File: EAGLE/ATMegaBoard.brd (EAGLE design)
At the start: 91.4 x 69.5 mm, 29 parts, among them IC1 L298, IC2 ATMEGA168-20P, IC3 REG1117, J1 1X2-3.5MM, J2 1X2-3.5MM, J3 1X2-3.5MM, J4 1X2-3.5MM, X1 49S/18PF

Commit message: added standalone board
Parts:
- removed U$1: (no value), heatsink:FK213
- added U$2: (no value), heatsink:D03S
- moved D5 56.7 mm to (22.9, 47.0), turned to 180 degrees
- moved J2 54.3 mm to (34.3, 44.5), turned to 180 degrees
- moved D6 51.4 mm to (22.9, 41.9), turned to 180 degrees
- moved J1 45.1 mm to (41.9, 44.5), turned to 180 degrees
- moved D2 19.7 mm to (57.1, 44.5), turned to 180 degrees
- moved D1 16.6 mm to (63.5, 49.5), turned to 180 degrees
- moved HC-SR04 16.5 mm to (5.08, 36.8), turned to 90 degrees
- moved IC3 16.2 mm to (43.2, 20.3), turned to 0 degrees
- moved C3 15.5 mm to (40.6, 12.7), turned to 180 degrees
- moved IC1 12.8 mm to (57.1, 33.0)
- moved HC05 11.7 mm to (11.4, 10.2)
- moved D3 11.5 mm to (64.8, 17.8)
- moved D4 11.5 mm to (69.8, 17.8)
- moved D7 11.5 mm to (54.6, 12.7)
- moved D8 11.5 mm to (61.0, 10.2)
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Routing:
- net +5V: track 121.8 -> 109.8 mm
- net OUT2: track 44.5 -> 35.9 mm
- net VIN: track 107.2 -> 114.4 mm
- net TX: track 9.20 -> 16.3 mm
- net PIN5HC05: track 4.34 -> 10.7 mm
- net ECHO: track 5.08 -> 9.72 mm
- net IN1: track 17.9 -> 13.4 mm
- net IN3: track 20.8 -> 17.0 mm
- net ENA: track 15.8 -> 12.0 mm
- net IN4: track 15.8 -> 12.0 mm
- net IN2: track 13.8 -> 9.94 mm
- net ENB: track 21.3 -> 17.5 mm
- net OUT4: track 29.0 -> 32.4 mm
- net OUT1: track 37.4 -> 39.6 mm
- net OUT3: track 41.6 -> 39.9 mm
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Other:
- board size 91.4 x 69.5 mm -> 81.3 x 51.7 mm

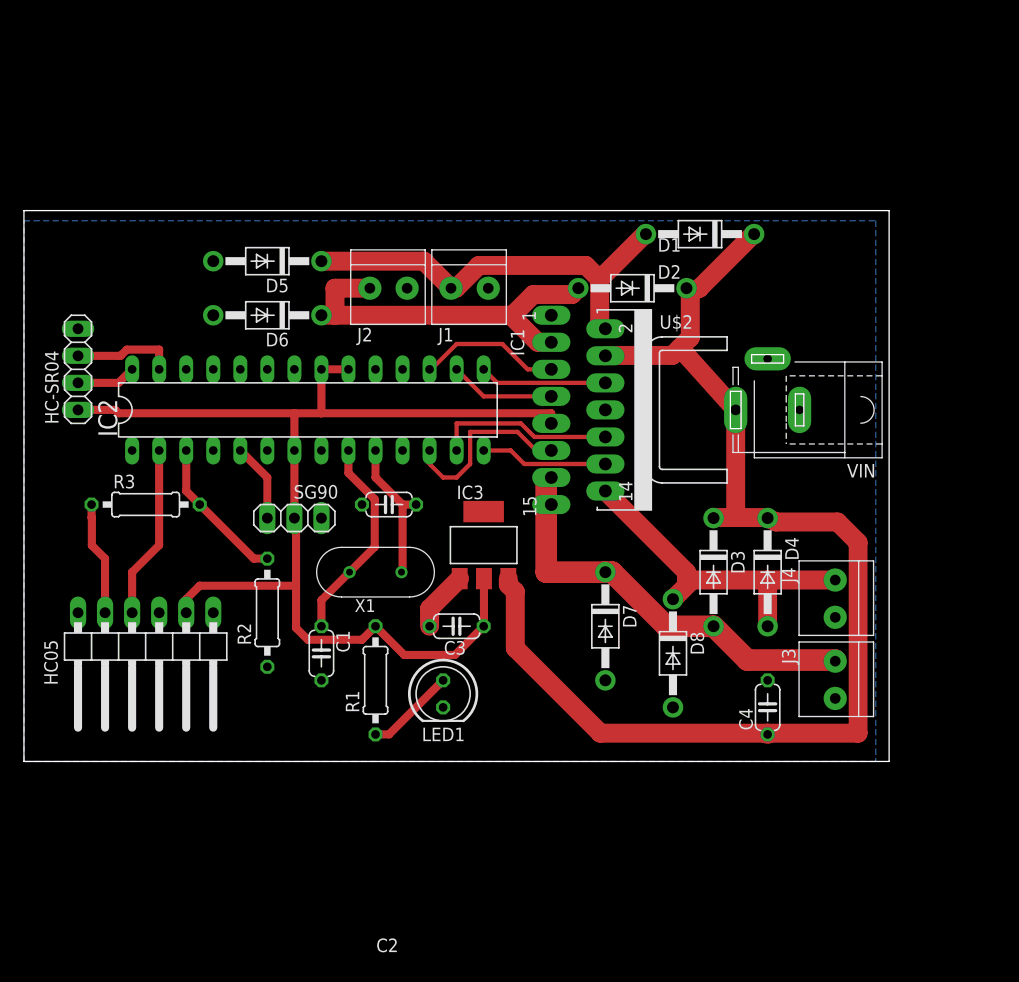
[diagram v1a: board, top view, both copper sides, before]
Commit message: updated ATMegaBoard, added CAM files
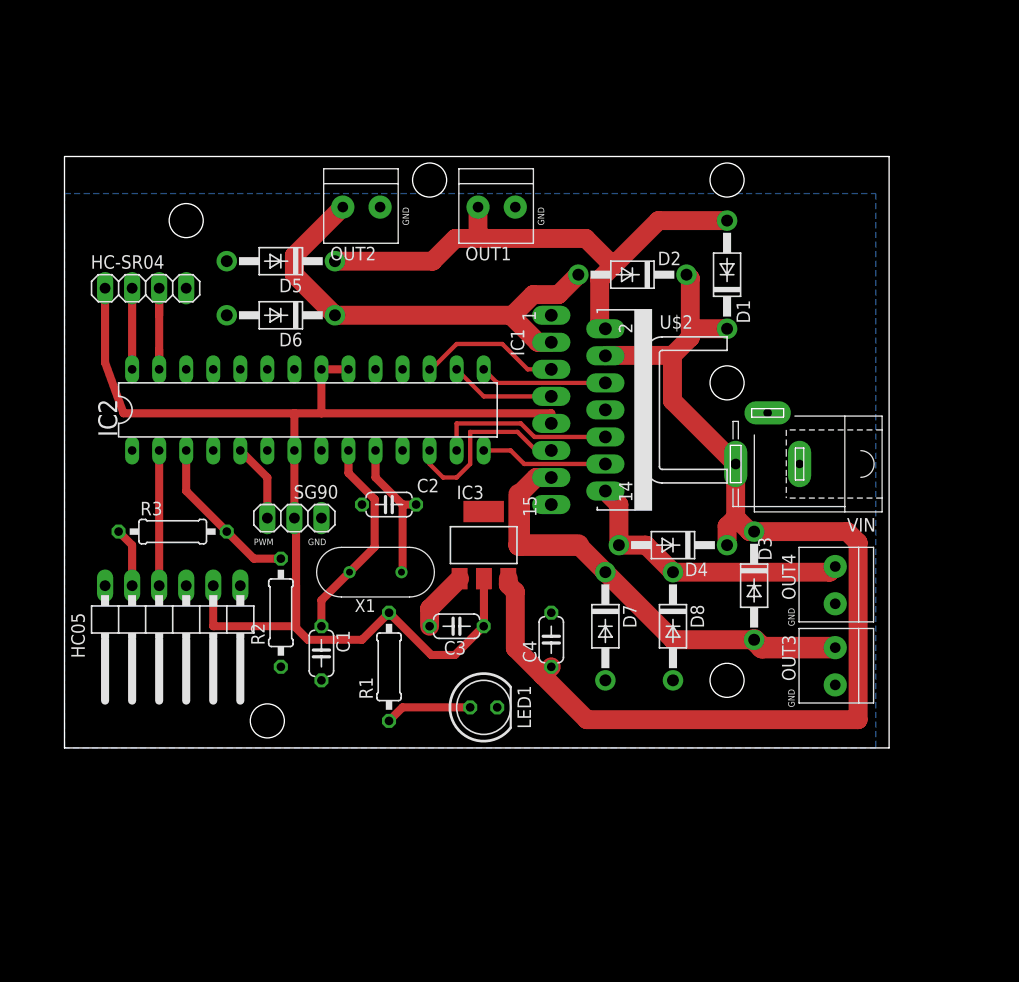
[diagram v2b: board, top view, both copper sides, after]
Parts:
- removed J1, J2, J3, J4: 1X2-3.5MM, adafruit:1X2-3.5MM
- added OUT1, OUT2, OUT3, OUT4: 1X2-3.5MM, adafruit:1X2-3.5MM
- moved C4 21.3 mm to (49.5, 11.4)
- moved HC-SR04 9.92 mm to (11.4, 44.5), turned to 0 degrees
- moved D4 9.25 mm to (61.0, 20.3), turned to 180 degrees
- moved VIN 5.08 mm to (69.8, 27.9)
- moved D1 4.58 mm to (66.0, 45.7), turned to 90 degrees
- moved D3 4.02 mm to (68.6, 16.5)
- moved LED1 4.02 mm to (43.2, 5.08), turned to 0 degrees
- moved HC05 3.59 mm to (14.0, 12.7)
- moved R3 3.59 mm to (14.0, 21.6)
- moved D8 2.54 mm to (61.0, 12.7)
- moved R1 1.80 mm to (34.3, 8.89)
- moved D5 1.27 mm to (24.1, 47.0)
- moved D6 1.27 mm to (24.1, 41.9)
- moved R2 1.27 mm to (24.1, 14.0)
- moved D2 1.27 mm to (57.1, 45.7)
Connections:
- net GND: now also OUT1.2, OUT2.2, OUT3.2, OUT4.2; no longer J1.2, J2.2, J3.2, J4.2
- net OUT1: now also OUT1.1; no longer J1.1
- net OUT2: now also OUT2.1; no longer J2.1
- net OUT3: now also OUT3.1; no longer J3.1
- net OUT4: now also OUT4.1; no longer J4.1
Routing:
- net +5V: track 109.8 -> 121.8 mm
- net OUT1: track 39.6 -> 50.4 mm
- net OUT2: track 35.9 -> 42.9 mm
- net OUT4: track 32.4 -> 27.2 mm
- net PIN5HC05: track 10.7 -> 5.61 mm
- net VIN: track 114.4 -> 110.8 mm
- net TX: track 16.3 -> 12.7 mm
- net ECHO: track 9.72 -> 12.0 mm
- net OUT3: track 39.9 -> 42.1 mm
- net TRIG: track 5.61 -> 7.62 mm
- net RX: track 14.1 -> 15.3 mm
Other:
- board size 81.3 x 51.7 mm -> 77.5 x 55.5 mm
- board text added: "GND"
- board text added: "PWM"

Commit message: Switched to female header for HC05
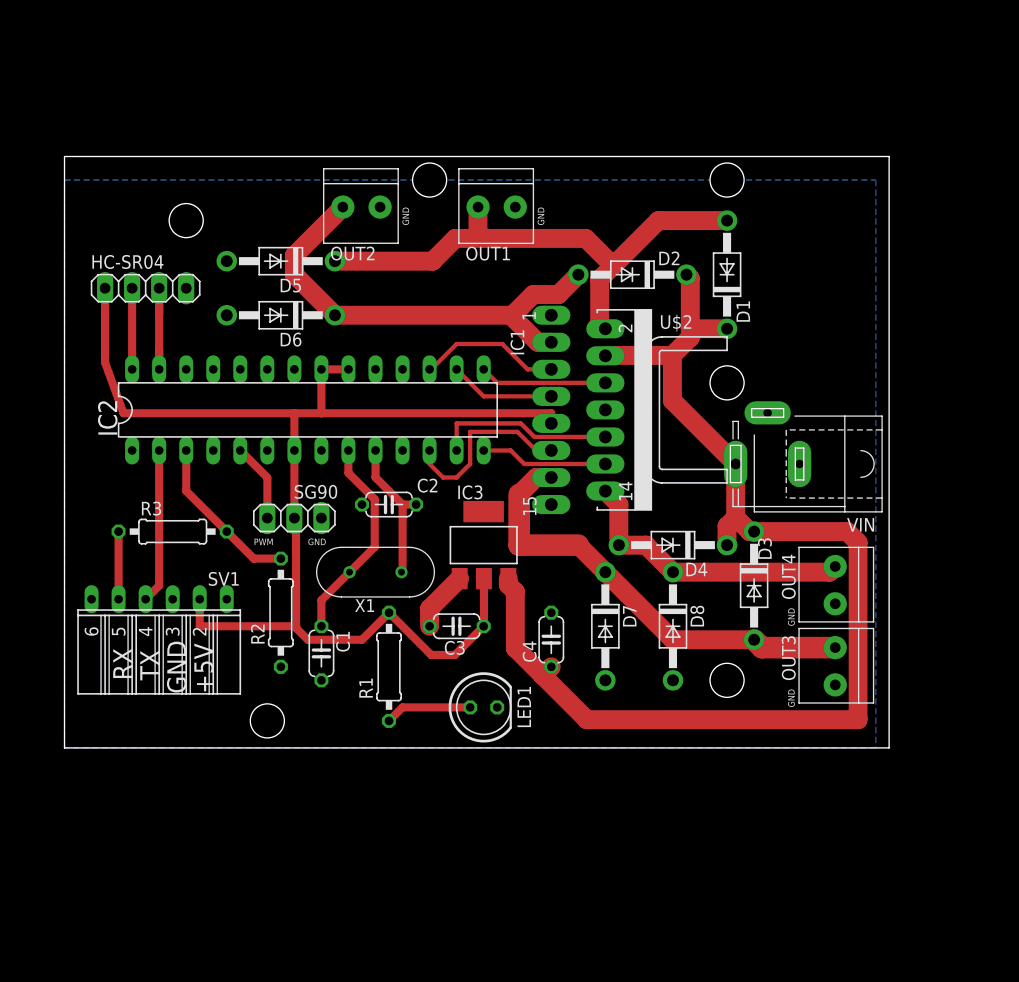
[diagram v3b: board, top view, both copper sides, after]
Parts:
- removed HC05: (no value), pinhead:1X06/90
- added SV1: (no value), con-lsta:FE06W
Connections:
- net +5V: now also SV1.2; no longer HC05.2
- net GND: now also SV1.3; no longer HC05.3
- net PIN5HC05: now also SV1.5; no longer HC05.5
- net TX: now also SV1.4; no longer HC05.4
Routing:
- net TX: track 12.7 -> 14.5 mm
- net PIN5HC05: track 5.61 -> 6.35 mm
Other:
- board text added: "+5V"
- board text added: "RX"
- board text added: "TX"
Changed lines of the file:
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@@
 <text x="48.26" y="52.07" size="0.6096" layer="21" rot="R270">GND</text>
 <text x="35.56" y="52.07" size="0.6096" layer="21" rot="R270">GND</text>
+<text x="10.16" y="7.62" size="1.778" layer="21" rot="R90">RX</text>
+<text x="12.7" y="7.62" size="1.778" layer="21" rot="R90">TX</text>
+<text x="15.24" y="6.35" size="1.778" layer="21" rot="R90">GND</text>
+<text x="17.78" y="6.35" size="1.778" layer="21" rot="R90">+5V</text>
 </plain>
 <attributes>
@@
 <attribute name="VALUE" x="6.35" y="41.275" size="1.27" layer="27"/>
 </element>
-<element name="HC05" library="pinhead" library_urn="urn:adsk.eagle:library:325" package="1X06/90" package3d_urn="urn:adsk.eagle:package:22475/2" value="" x="13.97" y="12.7" smashed="yes" rot="R180">
-<attribute name="NAME" x="4.445" y="13.97" size="1.27" layer="25" ratio="10" rot="R270"/>
-<attribute name="POPULARITY" value="10" x="-7.62" y="34.29" size="1.778" layer="27" rot="R180" display="off"/>
-<attribute name="VALUE" x="4.445" y="16.51" size="1.27" layer="27" rot="R270"/>
-</element>
 <element name="IC1" library="st-microelectronics" library_urn="urn:adsk.eagle:library:368" package="MULTIWATT-15" package3d_urn="urn:adsk.eagle:package:26823/1" value="L298" x="57.15" y="33.02" smashed="yes" rot="R270">
 <attribute name="MF" value="" x="43.18" y="8.89" size="1.778" layer="27" rot="R270" display="off"/>
@@
 <attribute name="NAME" x="59.69" y="40.64" size="1.27" layer="25" ratio="10"/>
 <attribute name="VALUE" x="59.69" y="24.13" size="1.27" layer="27" ratio="10"/>
+</element>
+<element name="SV1" library="con-lsta" library_urn="urn:adsk.eagle:library:161" package="FE06W" package3d_urn="urn:adsk.eagle:package:8198/1" value="" x="12.7" y="15.24" smashed="yes" rot="R180">
+<attribute name="MF" value="" x="12.7" y="15.24" size="1.778" layer="27" rot="R180" display="off"/>
+<attribute name="MPN" value="" x="12.7" y="15.24" size="1.778" layer="27" rot="R180" display="off"/>
+<attribute name="NAME" x="20.32" y="17.78" size="1.27" layer="25" ratio="10" rot="R180"/>
+<attribute name="OC_FARNELL" value="unknown" x="12.7" y="15.24" size="1.778" layer="27" rot="R180" display="off"/>
+<attribute name="OC_NEWARK" value="unknown" x="12.7" y="15.24" size="1.778" layer="27" rot="R180" display="off"/>
+<attribute name="POPULARITY" value="3" x="12.7" y="15.24" size="1.778" layer="27" rot="R180" display="off"/>
+<attribute name="VALUE" x="18.542" y="13.208" size="1.27" layer="27" ratio="10" rot="R270"/>
 </element>
 </elements>
@@
 </signal>
 <signal name="TX">
-<contactref element="HC05" pad="4"/>
 <contactref element="IC2" pad="2"/>
+<contactref element="SV1" pad="4"/>
 <wire x1="12.7" y1="29.21" x2="12.7" y2="16.51" width="0.762" layer="1"/>
+<wire x1="12.7" y1="16.51" x2="11.43" y2="15.24" width="0.762" layer="1"/>
 </signal>
 <signal name="+5V" class="2">
-<contactref element="HC05" pad="2"/>
 <contactref element="IC2" pad="7"/>
 <contactref element="IC2" pad="21"/>
@@
 <wire x1="27.94" y1="36.83" x2="30.48" y2="36.83" width="0.762" layer="1"/>
 <wire x1="25.4" y1="29.21" x2="25.4" y2="32.7025" width="0.762" layer="1"/>
-<wire x1="25.55875" y1="12.7" x2="17.78" y2="12.7" width="0.762" layer="1"/>
-<wire x1="17.78" y1="16.51" x2="17.78" y2="12.7" width="0.762" layer="1"/>
+<wire x1="16.51" y1="12.7" x2="25.55875" y2="12.7" width="0.762" layer="1"/>
 <wire x1="34.29" y1="13.97" x2="31.75" y2="11.43" width="0.762" layer="1"/>
 <wire x1="31.75" y1="11.43" x2="26.67" y2="11.43" width="0.762" layer="1"/>
@@
 <wire x1="43.18" y1="12.7" x2="43.2054" y2="12.7254" width="0.762" layer="1"/>
 <wire x1="43.2054" y1="17.1704" x2="43.2054" y2="12.7254" width="0.762" layer="1"/>
+<contactref element="SV1" pad="2"/>
+<wire x1="16.51" y1="15.24" x2="16.51" y2="12.7" width="0.762" layer="1"/>
 <wire x1="25.4" y1="22.86" x2="25.55875" y2="16.51" width="0" layer="19" extent="1-1"/>
 </signal>
 <signal name="GND" class="1">
-<contactref element="HC05" pad="3"/>
 <contactref element="IC2" pad="8"/>
 <contactref element="C1" pad="2"/>
@@
 <contactref element="R2" pad="1"/>
 <polygon width="0.1524" layer="16">
-<vertex x="3.81" y="53.34"/>
-<vertex x="80.01" y="53.34"/>
+<vertex x="3.81" y="54.61"/>
+<vertex x="80.01" y="54.61"/>
 <vertex x="80.01" y="1.27"/>
 <vertex x="3.81" y="1.27"/>
@@
 <wire x1="38.1" y1="12.7" x2="38.1" y2="14.351" width="1.778" layer="1"/>
 <wire x1="38.1" y1="14.351" x2="40.9194" y2="17.1704" width="1.778" layer="1"/>
+<contactref element="SV1" pad="3"/>
 </signal>
 <signal name="VIN" class="1">
@@
 </signal>
 <signal name="PIN5HC05">
-<contactref element="HC05" pad="5"/>
+<contactref element="SV1" pad="5"/>
 <contactref element="R3" pad="1"/>
-<wire x1="10.16" y1="16.51" x2="10.16" y2="20.32" width="0.762" layer="1"/>
-<wire x1="10.16" y1="20.32" x2="8.89" y2="21.59" width="0.762" layer="1"/>
+<wire x1="8.89" y1="15.24" x2="8.89" y2="21.59" width="0.762" layer="1"/>
 </signal>
 </signals>

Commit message: compressed board
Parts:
- removed SV1: (no value), con-lsta:FE06W
- added HC05: (no value), con-lsta:FE06W
- moved VIN 18.5 mm to (64.8, 45.7)
- moved D1 15.7 mm to (50.8, 49.5), turned to 180 degrees
- moved D5 13.0 mm to (36.8, 44.5)
- moved D2 7.62 mm to (49.5, 45.7)
- moved C4 6.35 mm to (49.5, 5.08), turned to 0 degrees
- moved OUT1 4.02 mm to (40.6, 50.8)
- moved OUT3 4.02 mm to (72.4, 7.62)
- moved D3 3.81 mm to (64.8, 16.5)
- moved D4 3.81 mm to (57.1, 20.3)
- moved D7 3.81 mm to (50.8, 12.7)
- moved D8 3.81 mm to (57.1, 12.7)
- moved LED1 3.81 mm to (39.4, 5.08)
- moved OUT4 3.81 mm to (72.4, 16.5)
- moved D6 2.54 mm to (26.7, 41.9)
- moved C1 2.54 mm to (30.5, 10.2)
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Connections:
- net +5V: now also HC05.2; no longer SV1.2
- net GND: now also HC05.3; no longer SV1.3
- net PIN5HC05: now also HC05.5; no longer SV1.5
- net TX: now also HC05.4; no longer SV1.4
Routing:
- net OUT1: track 50.4 -> 26.0 mm
- net VIN: track 110.8 -> 122.1 mm
- net OUT2: track 42.9 -> 34.3 mm
- net OUT3: track 42.1 -> 37.8 mm
- net +5V: track 121.8 -> 117.9 mm
- net N$3: track 8.15 -> 4.34 mm
- net RX: track 15.3 -> 17.1 mm
- net ECHO: track 12.0 -> 10.7 mm
- net XTAL1: track 19.6 -> 18.6 mm
- net PIN5HC05: track 6.35 -> 7.40 mm
- net TRIG: track 7.62 -> 8.15 mm
- net OUT4: track 27.2 -> 27.7 mm
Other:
- board size 77.5 x 55.5 mm -> 71.1 x 54.3 mm

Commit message: minor board updates
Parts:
- added LIGHTS: (no value), con-lstb:MA05-2
- moved C4 7.73 mm to (41.9, 3.81)
- moved C1 6.48 mm to (24.1, 8.89)
- moved C3 6.48 mm to (34.3, 11.4)
- moved D4 6.48 mm to (50.8, 19.1)
- moved D8 6.48 mm to (50.8, 11.4)
- moved IC1 6.48 mm to (50.8, 31.8)
- moved IC2 6.48 mm to (20.3, 31.8)
- moved IC3 6.48 mm to (36.8, 19.1)
- moved X1 6.48 mm to (26.7, 16.5)
- moved R3 6.48 mm to (7.62, 20.3)
- moved HC-SR04 6.48 mm to (6.35, 43.2)
- moved HC05 6.48 mm to (8.89, 14.0)
- moved C2 6.48 mm to (27.9, 22.9)
- moved R1 6.48 mm to (27.9, 7.62)
- moved R2 6.48 mm to (19.1, 11.4)
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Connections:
- new net N$1: IC2.23, LIGHTS.3, LIGHTS.4
- new net N$2: IC2.24, LIGHTS.5, LIGHTS.6
- new net N$4: IC2.25, LIGHTS.7, LIGHTS.8
- new net N$5: IC2.26, LIGHTS.10, LIGHTS.9
- net +5V: now also IC2.1
- net GND: now also LIGHTS.1, LIGHTS.2
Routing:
- net N$4: track 0.00 -> 16.1 mm
- net N$5: track 0.00 -> 16.1 mm
- net N$2: track 0.00 -> 16.1 mm
- net N$1: track 0.00 -> 16.1 mm
- net VIN: track 122.1 -> 118.5 mm
- net ECHO: track 10.7 -> 8.15 mm
- net OUT2: track 34.3 -> 32.2 mm
- net XTAL1: track 18.6 -> 16.6 mm
- net OUT1: track 26.0 -> 24.1 mm
- net IN3: track 17.0 -> 16.3 mm
- net +5V: track 117.9 -> 118.5 mm
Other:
- outline, holes or cut-outs redrawn
- board text added: "OUT1"
- board text added: "OUT2"
- board text added: "OUT3"
- board text added: "OUT4"
- board text added: "PC0"
- board text added: "PC1"
- board text added: "PC2"
- board text added: "PC3"
